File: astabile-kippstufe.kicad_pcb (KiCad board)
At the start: 2 copper layers, 57 x 32 mm, 16 parts, among them X1 +UB, X2 0V

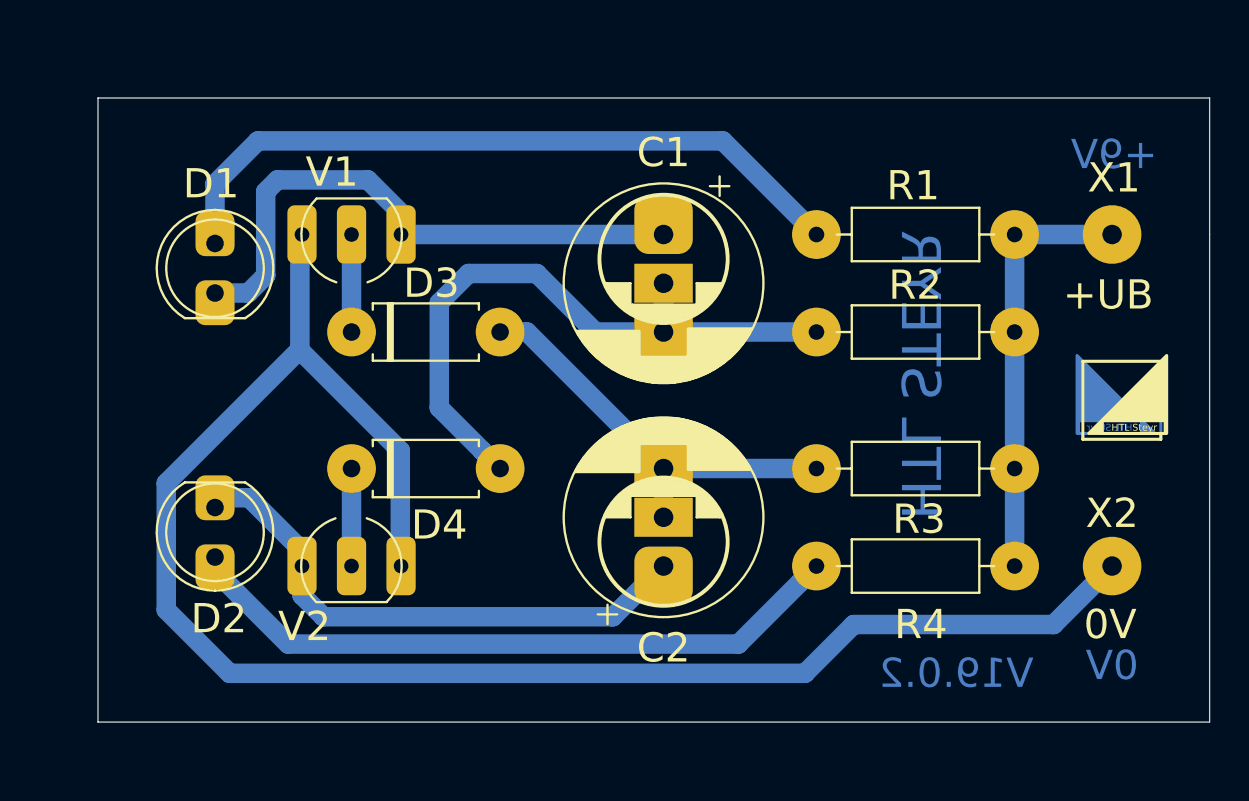
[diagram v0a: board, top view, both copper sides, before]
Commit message: wires modified and mounting holes
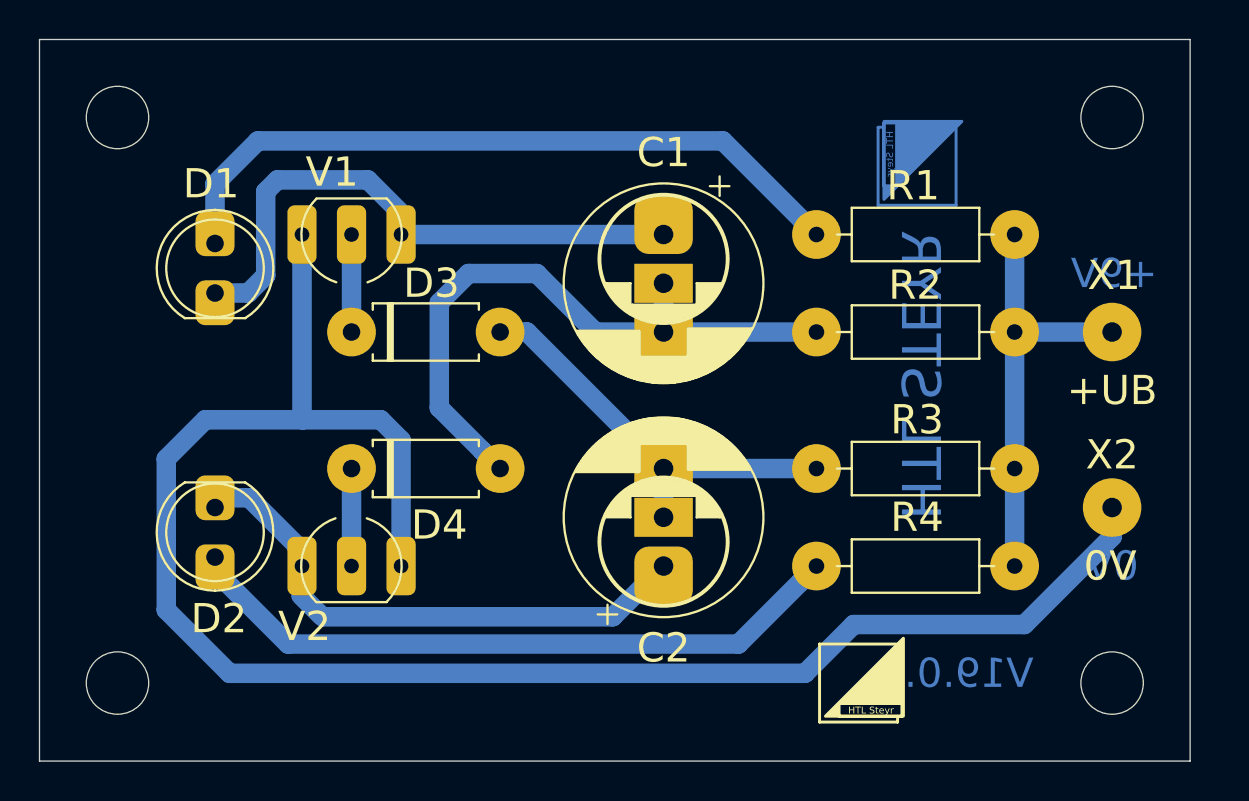
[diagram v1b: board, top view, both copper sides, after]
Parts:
- added H1: MountingHole, MountingHole:MountingHole_3.2mm_M3, F.Cu at (175.0, 69.0)
- added H2: MountingHole, MountingHole:MountingHole_3.2mm_M3, F.Cu at (175.0, 98.0)
- added H3: MountingHole, MountingHole:MountingHole_3.2mm_M3, F.Cu at (124.0, 69.0)
- added H4: MountingHole, MountingHole:MountingHole_3.2mm_M3, F.Cu at (124.0, 98.0)
- moved Logo1 19.8 mm to (162.0, 98.0)
- moved Logo2 15.9 mm to (165.0, 71.5), turned to 90 degrees
- moved X1 5.00 mm to (175.0, 80.0)
- moved X2 3.00 mm to (175.0, 89.0)
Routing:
- net Net-(V1-Pad3): track 87.5 -> 92.6 mm
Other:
- board size 57 x 32 mm -> 59 x 37 mm
